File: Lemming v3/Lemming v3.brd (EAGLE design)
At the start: 29.5 x 19.1 mm, 37 parts, among them IC1 ADAFRUIT_SENSOR_PCF8574RGY, U1 SIP32431DR3-T1GE3, U2 SIP32431DR3-T1GE3, U3 SIP32431DR3-T1GE3, U4 SIP32431DR3-T1GE3, U5 SIP32431DR3-T1GE3, U6 SIP32431DR3-T1GE3, U7 SIP32431DR3-T1GE3, U8 SIP32431DR3-T1GE3

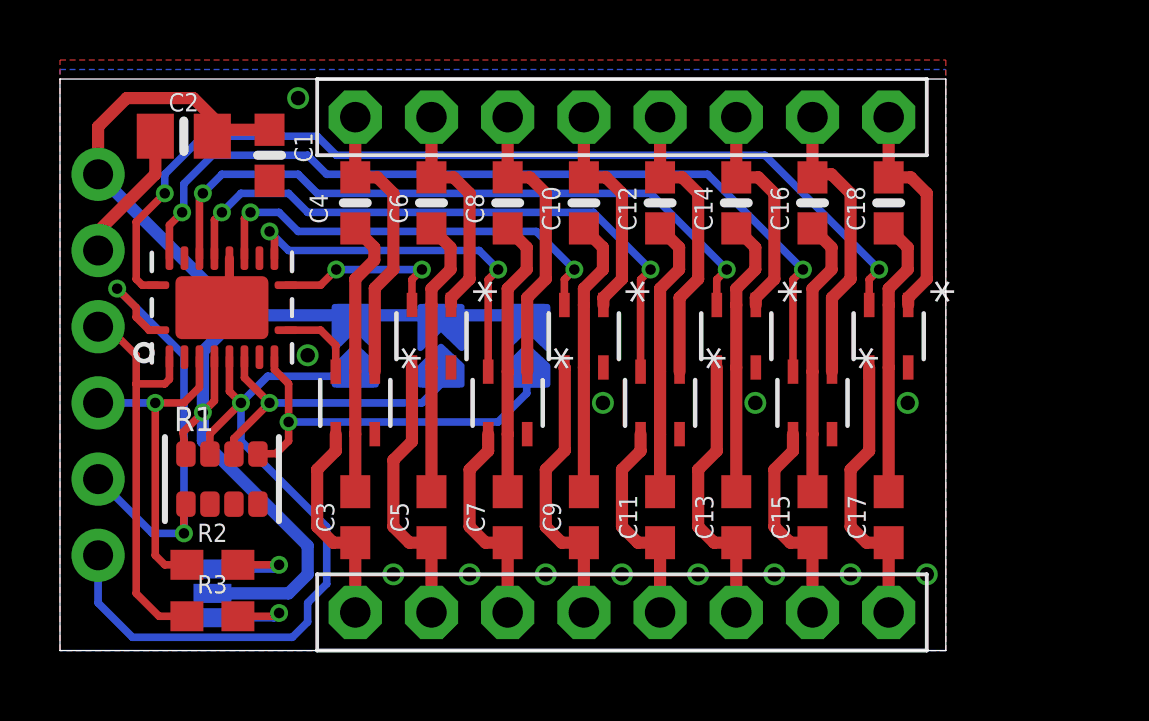
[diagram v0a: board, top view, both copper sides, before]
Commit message: Added two more switches with external control
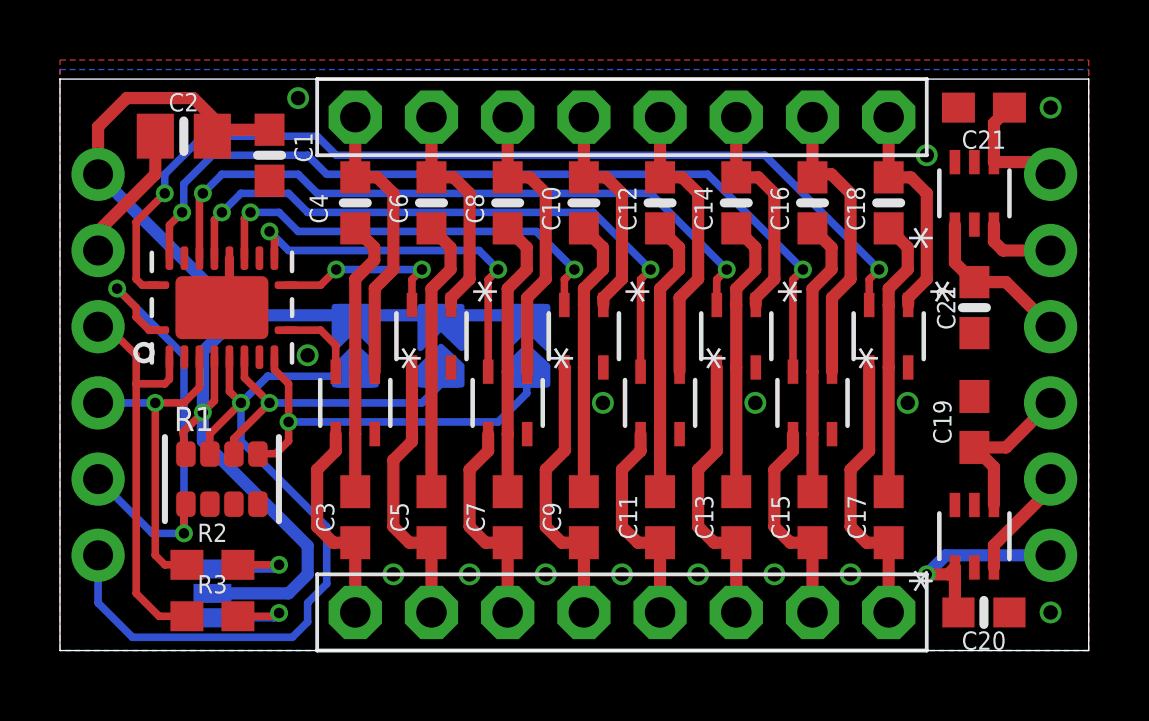
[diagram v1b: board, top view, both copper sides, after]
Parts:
- added C19, C21: 1.0uF, SparkFun-Capacitors:0603
- added C20, C22: 0.1uF, microbuilder:0603-NO
- added JP5: (no value), microbuilder:1X06_ROUND_70
- added U10, U9: SIP32431DR3-T1GE3, Switch:SC-70-6_VIS
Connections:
- new net IN8: C19.1, JP5.3, U9.4
- new net IN9: C21.1, JP5.6, U10.4
- new net OUT8: C20.1, JP5.1, U9.1
- new net OUT9: C22.1, JP5.4, U10.1
- new net P8: JP5.2, U9.3
- new net P9: JP5.5, U10.3
- net GND: now also C19.2, C20.2, C21.2, C22.2, U10.2, U10.5, U9.2, U9.5
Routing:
- net OUT8: track 0.00 -> 6.97 mm, vias 0 -> 1
- net OUT9: track 0.00 -> 5.34 mm
- net IN8: track 0.00 -> 5.34 mm
- net IN9: track 0.00 -> 4.09 mm
- net P8: track 0.00 -> 3.73 mm
- net P9: track 0.00 -> 2.58 mm
- net GND: vias 13 -> 15
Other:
- board size 29.5 x 19.1 mm -> 34.3 x 19.1 mm
- board text added: "IN8"
- board text added: "IN9"
- board text added: "OUT8"
- board text added: "OUT9"
- board text added: "P8"
- board text added: "P9"

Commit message: CR1000X Boards
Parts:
- moved JP5 0.32 mm to (32.7, 9.53)
- moved C19 0.32 mm to (30.2, 7.62)
- moved C21 0.32 mm to (30.8, 17.8)
- moved C22 0.32 mm to (30.2, 11.4)
- moved U10 0.32 mm to (30.2, 15.2)
- moved U9 0.32 mm to (30.2, 3.81)
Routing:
- net GND: track 80.8 -> 82.4 mm, vias 15 -> 14
- net OUT8: track 6.97 -> 6.47 mm
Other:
- board size 34.3 x 19.1 mm -> 34 x 19.1 mm
